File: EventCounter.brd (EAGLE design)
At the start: 38.1 x 19.6 mm, 23 parts, among them J1 CONN_42.54_SCREW, Q1 2N7002, Q3 DMG3404, U7 MCP6041, U8 MCP6041

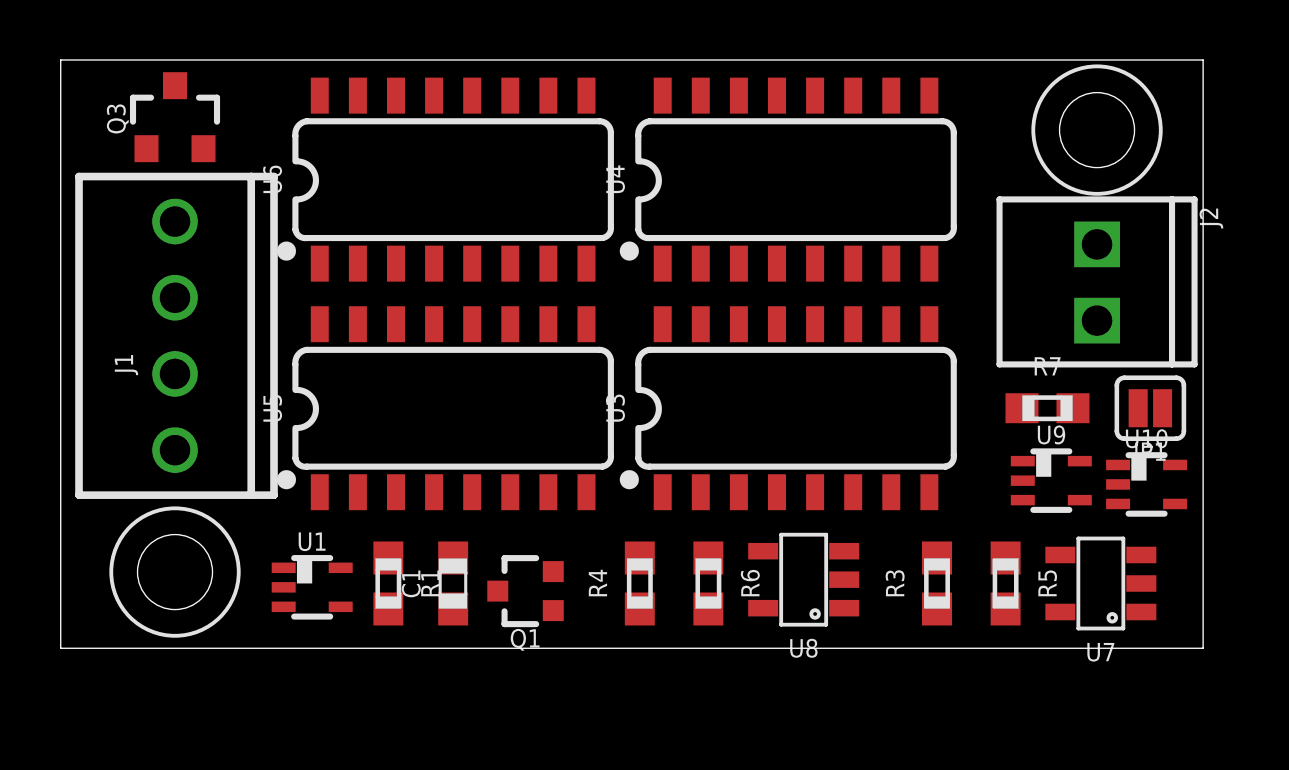
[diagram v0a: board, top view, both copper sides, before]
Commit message: Completed initial routing, added silk screen info
Board is functionally complete baring cleanup or modifications, added silk screen info to bottom layer
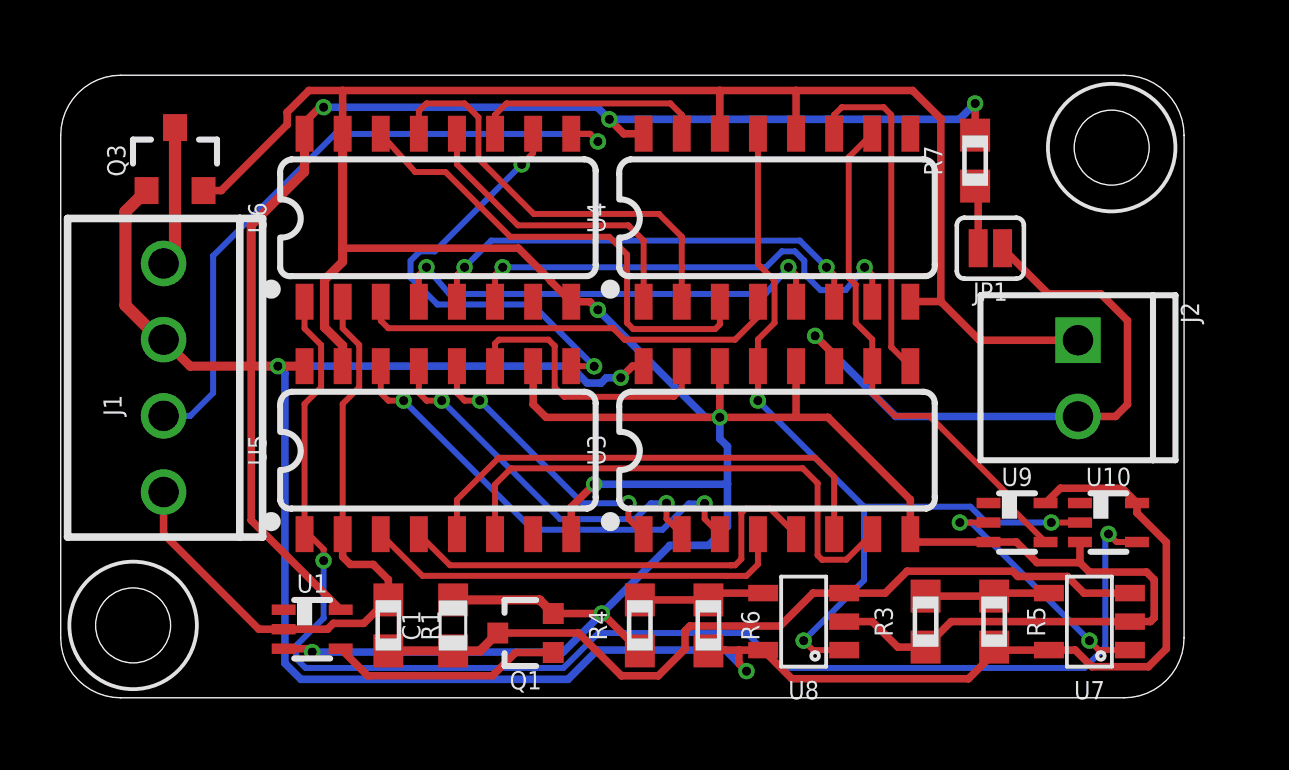
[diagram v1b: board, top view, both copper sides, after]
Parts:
- moved R7 8.60 mm to (30.5, 17.9), turned to 90 degrees
- moved JP1 7.54 mm to (31.0, 15.0)
- moved J2 4.51 mm to (33.9, 10.6)
- moved H1 2.26 mm to (2.41, 2.41)
- moved U9 1.81 mm to (31.9, 5.84)
- moved U10 1.80 mm to (34.9, 5.84)
- moved U3 1.53 mm to (23.9, 8.26)
- moved U5 1.49 mm to (12.6, 8.26)
- moved J1 1.45 mm to (3.43, 10.7)
- moved U4 1.42 mm to (23.9, 16.0)
- moved C1 1.40 mm to (13.1, 2.41)
- moved Q1 1.40 mm to (15.5, 2.16)
- moved R1 1.40 mm to (10.9, 2.41)
- moved R4 1.40 mm to (19.3, 2.41)
- moved R6 1.40 mm to (21.6, 2.41)
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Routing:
- net GND: track 0.00 -> 141.7 mm, vias 0 -> 5
- net VCC: track 0.00 -> 119.7 mm, vias 0 -> 6
- net LOAD: track 0.00 -> 46.4 mm, vias 0 -> 2
- net !LOAD: track 0.00 -> 28.6 mm, vias 0 -> 3
- net RC_OUT: track 0.00 -> 27.7 mm
- net CLK: track 0.00 -> 22.5 mm
- net DATA: track 0.00 -> 22.2 mm, vias 0 -> 1
- net PULSE: track 0.00 -> 21.0 mm, vias 0 -> 1
- net N$9: track 0.00 -> 17.5 mm
- net !RST: track 0.00 -> 17.3 mm
- net N$10: track 0.00 -> 16.5 mm
- net N$4: track 0.00 -> 16.2 mm
- net N$8: track 0.00 -> 15.9 mm, vias 0 -> 2
- net N$6: track 0.00 -> 15.4 mm, vias 0 -> 2
- net N$7: track 0.00 -> 15.3 mm, vias 0 -> 2
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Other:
- board size 38.1 x 19.6 mm -> 37.4 x 20.8 mm
- board text added: "Clk"
- board text added: "Data"
- board text added: "GND"
- board text added: "J0"
- board text added: "Project Tally v0.0 -------------- Developed by Northern Widget and University of Minnesota"
- board text added: "Pulse"
- board text added: "To Logger 3.3v ~ 5v"
- board text added: "To Sensor"
- board text added: "Vcc"

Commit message: Changed passive values
Changed the passive resistor divider values, need to verify with part availability
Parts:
- R3, R4, R5: value 10k -> 10M
- R6: value 30k -> 30M
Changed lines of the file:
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@@
 <attribute name="VALUE_PART" value="10k" x="10.922" y="2.413" size="1.778" layer="27" rot="R270" display="off"/>
 </element>
-<element name="R3" library="bschulz_passives" package="R0603" value="10k" x="28.829" y="2.54" rot="R90">
+<element name="R3" library="bschulz_passives" package="R0603" value="10M" x="28.829" y="2.54" rot="R90">
 <attribute name="DIGIKEY" value="311-10.0KHRCT-ND" x="28.829" y="2.54" size="1.778" layer="27" rot="R90" display="off"/>
 <attribute name="MF" value="Yageo" x="28.829" y="2.54" size="1.778" layer="27" rot="R90" display="off"/>
@@
 <attribute name="VALUE_PART" value="10k" x="28.829" y="2.54" size="1.778" layer="27" rot="R90" display="off"/>
 </element>
-<element name="R4" library="bschulz_passives" package="R0603" value="10k" x="19.304" y="2.413" rot="R90">
+<element name="R4" library="bschulz_passives" package="R0603" value="10M" x="19.304" y="2.413" rot="R90">
 <attribute name="DIGIKEY" value="311-10.0KHRCT-ND" x="19.304" y="2.413" size="1.778" layer="27" rot="R90" display="off"/>
 <attribute name="MF" value="Yageo" x="19.304" y="2.413" size="1.778" layer="27" rot="R90" display="off"/>
@@
 <attribute name="VALUE_PART" value="10k" x="19.304" y="2.413" size="1.778" layer="27" rot="R90" display="off"/>
 </element>
-<element name="R5" library="bschulz_passives" package="R0603" value="10k" x="31.115" y="2.54" rot="R270">
+<element name="R5" library="bschulz_passives" package="R0603" value="10M" x="31.115" y="2.54" rot="R270">
 <attribute name="DIGIKEY" value="" x="31.115" y="2.54" size="1.778" layer="27" rot="R270" display="off"/>
 <attribute name="MF" value="Yageo" x="31.115" y="2.54" size="1.778" layer="27" rot="R270" display="off"/>
@@
 <attribute name="VALUE_PART" value="" x="31.115" y="2.54" size="1.778" layer="27" rot="R270" display="off"/>
 </element>
-<element name="R6" library="bschulz_passives" package="R0603" value="30k" x="21.59" y="2.413" rot="R270">
+<element name="R6" library="bschulz_passives" package="R0603" value="30M" x="21.59" y="2.413" rot="R270">
 <attribute name="DIGIKEY" value="" x="21.59" y="2.413" size="1.778" layer="27" rot="R270" display="off"/>
 <attribute name="MF" value="Yageo" x="21.59" y="2.413" size="1.778" layer="27" rot="R270" display="off"/>

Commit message: Changed resistor divider values for low power
After checking part availability, changed values to more logical ones
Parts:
- R4: value 10M -> 3.3M
- R6: value 30M -> 10M
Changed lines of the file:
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@@
 </element>
 <element name="R3" library="bschulz_passives" package="R0603" value="10M" x="28.829" y="2.54" rot="R90">
-<attribute name="DIGIKEY" value="311-10.0KHRCT-ND" x="28.829" y="2.54" size="1.778" layer="27" rot="R90" display="off"/>
+<attribute name="DIGIKEY" value="311-10.0MHRCT-ND" x="28.829" y="2.54" size="1.778" layer="27" rot="R90" display="off"/>
 <attribute name="MF" value="Yageo" x="28.829" y="2.54" size="1.778" layer="27" rot="R90" display="off"/>
-<attribute name="MPN" value="RC0603FR-0710KL" x="28.829" y="2.54" size="1.778" layer="27" rot="R90" display="off"/>
-<attribute name="VALUE_PART" value="10k" x="28.829" y="2.54" size="1.778" layer="27" rot="R90" display="off"/>
+<attribute name="MPN" value="RC0603FR-0710ML" x="28.829" y="2.54" size="1.778" layer="27" rot="R90" display="off"/>
+<attribute name="VALUE_PART" value="10M" x="28.829" y="2.54" size="1.778" layer="27" rot="R90" display="off"/>
 </element>
-<element name="R4" library="bschulz_passives" package="R0603" value="10M" x="19.304" y="2.413" rot="R90">
-<attribute name="DIGIKEY" value="311-10.0KHRCT-ND" x="19.304" y="2.413" size="1.778" layer="27" rot="R90" display="off"/>
-<attribute name="MF" value="Yageo" x="19.304" y="2.413" size="1.778" layer="27" rot="R90" display="off"/>
-<attribute name="MPN" value="RC0603FR-0710KL" x="19.304" y="2.413" size="1.778" layer="27" rot="R90" display="off"/>
-<attribute name="VALUE_PART" value="10k" x="19.304" y="2.413" size="1.778" layer="27" rot="R90" display="off"/>
+<element name="R4" library="bschulz_passives" package="R0603" value="3.3M" x="19.304" y="2.413" rot="R90">
+<attribute name="DIGIKEY" value="RMCF0603FT3M30CT-ND" x="19.304" y="2.413" size="1.778" layer="27" rot="R90" display="off"/>
+<attribute name="MF" value="Stackpole" x="19.304" y="2.413" size="1.778" layer="27" rot="R90" display="off"/>
+<attribute name="MPN" value="RMCF0603FT3M30" x="19.304" y="2.413" size="1.778" layer="27" rot="R90" display="off"/>
+<attribute name="VALUE_PART" value="3.3M" x="19.304" y="2.413" size="1.778" layer="27" rot="R90" display="off"/>
 </element>
 <element name="R5" library="bschulz_passives" package="R0603" value="10M" x="31.115" y="2.54" rot="R270">
-<attribute name="DIGIKEY" value="" x="31.115" y="2.54" size="1.778" layer="27" rot="R270" display="off"/>
+<attribute name="DIGIKEY" value="311-10.0MHRCT-ND" x="31.115" y="2.54" size="1.778" layer="27" rot="R270" display="off"/>
 <attribute name="MF" value="Yageo" x="31.115" y="2.54" size="1.778" layer="27" rot="R270" display="off"/>
-<attribute name="MPN" value="" x="31.115" y="2.54" size="1.778" layer="27" rot="R270" display="off"/>
-<attribute name="VALUE_PART" value="" x="31.115" y="2.54" size="1.778" layer="27" rot="R270" display="off"/>
+<attribute name="MPN" value="RC0603FR-0710ML" x="31.115" y="2.54" size="1.778" layer="27" rot="R270" display="off"/>
+<attribute name="VALUE_PART" value="10M" x="31.115" y="2.54" size="1.778" layer="27" rot="R270" display="off"/>
 </element>
-<element name="R6" library="bschulz_passives" package="R0603" value="30M" x="21.59" y="2.413" rot="R270">
-<attribute name="DIGIKEY" value="" x="21.59" y="2.413" size="1.778" layer="27" rot="R270" display="off"/>
+<element name="R6" library="bschulz_passives" package="R0603" value="10M" x="21.59" y="2.413" rot="R270">
+<attribute name="DIGIKEY" value="311-10.0MHRCT-ND" x="21.59" y="2.413" size="1.778" layer="27" rot="R270" display="off"/>
 <attribute name="MF" value="Yageo" x="21.59" y="2.413" size="1.778" layer="27" rot="R270" display="off"/>
-<attribute name="MPN" value="" x="21.59" y="2.413" size="1.778" layer="27" rot="R270" display="off"/>
-<attribute name="VALUE_PART" value="" x="21.59" y="2.413" size="1.778" layer="27" rot="R270" display="off"/>
+<attribute name="MPN" value="RC0603FR-0710ML" x="21.59" y="2.413" size="1.778" layer="27" rot="R270" display="off"/>
+<attribute name="VALUE_PART" value="10M" x="21.59" y="2.413" size="1.778" layer="27" rot="R270" display="off"/>
 </element>
 <element name="U1" library="bschulz" package="DCK_R-PDSO-G5" value="" x="8.382" y="2.286" rot="R270">

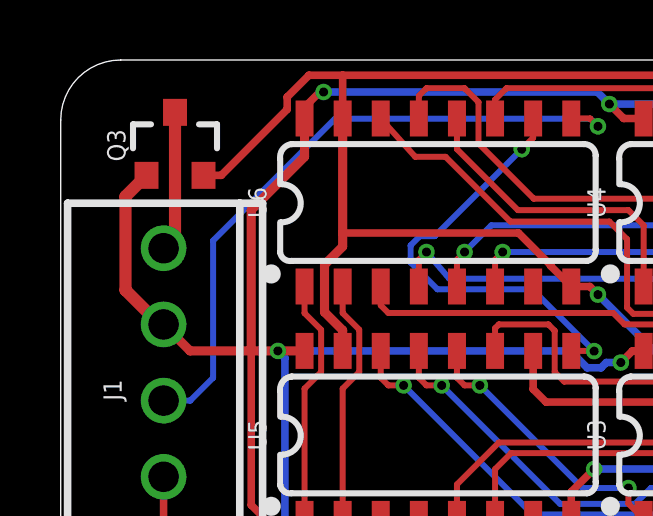
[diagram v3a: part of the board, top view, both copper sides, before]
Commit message: Added BOM and decoupling cap
Added BOM files and decoupling capacitor, cleaned up some silkscreen issues, ready for final review
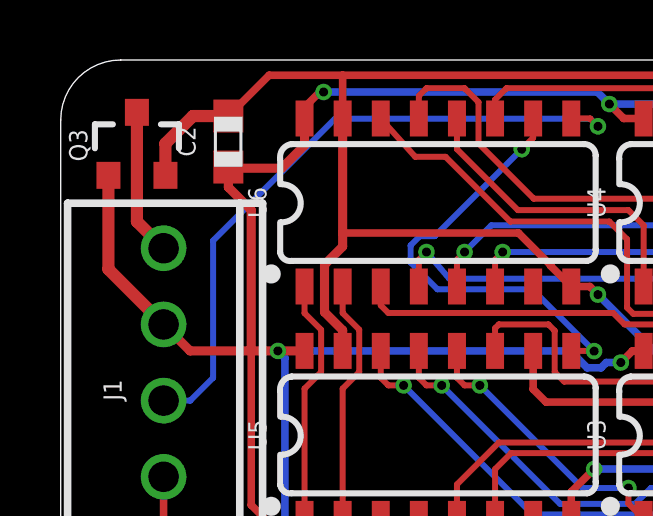
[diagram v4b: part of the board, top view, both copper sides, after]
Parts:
- added C2: 0.1uF, bschulz_passives:C0603
- moved Q3 1.27 mm to (2.54, 17.9)
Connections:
- net GND: now also C2.2
- net VCC: now also C2.1
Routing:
- net GND: track 141.7 -> 143.3 mm
- net VCC: track 119.7 -> 121.2 mm
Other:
- board text added: "To Sensor 0v ~ Vcc"
- board text removed: "To Sensor"
